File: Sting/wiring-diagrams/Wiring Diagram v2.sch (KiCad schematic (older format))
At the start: 14 parts

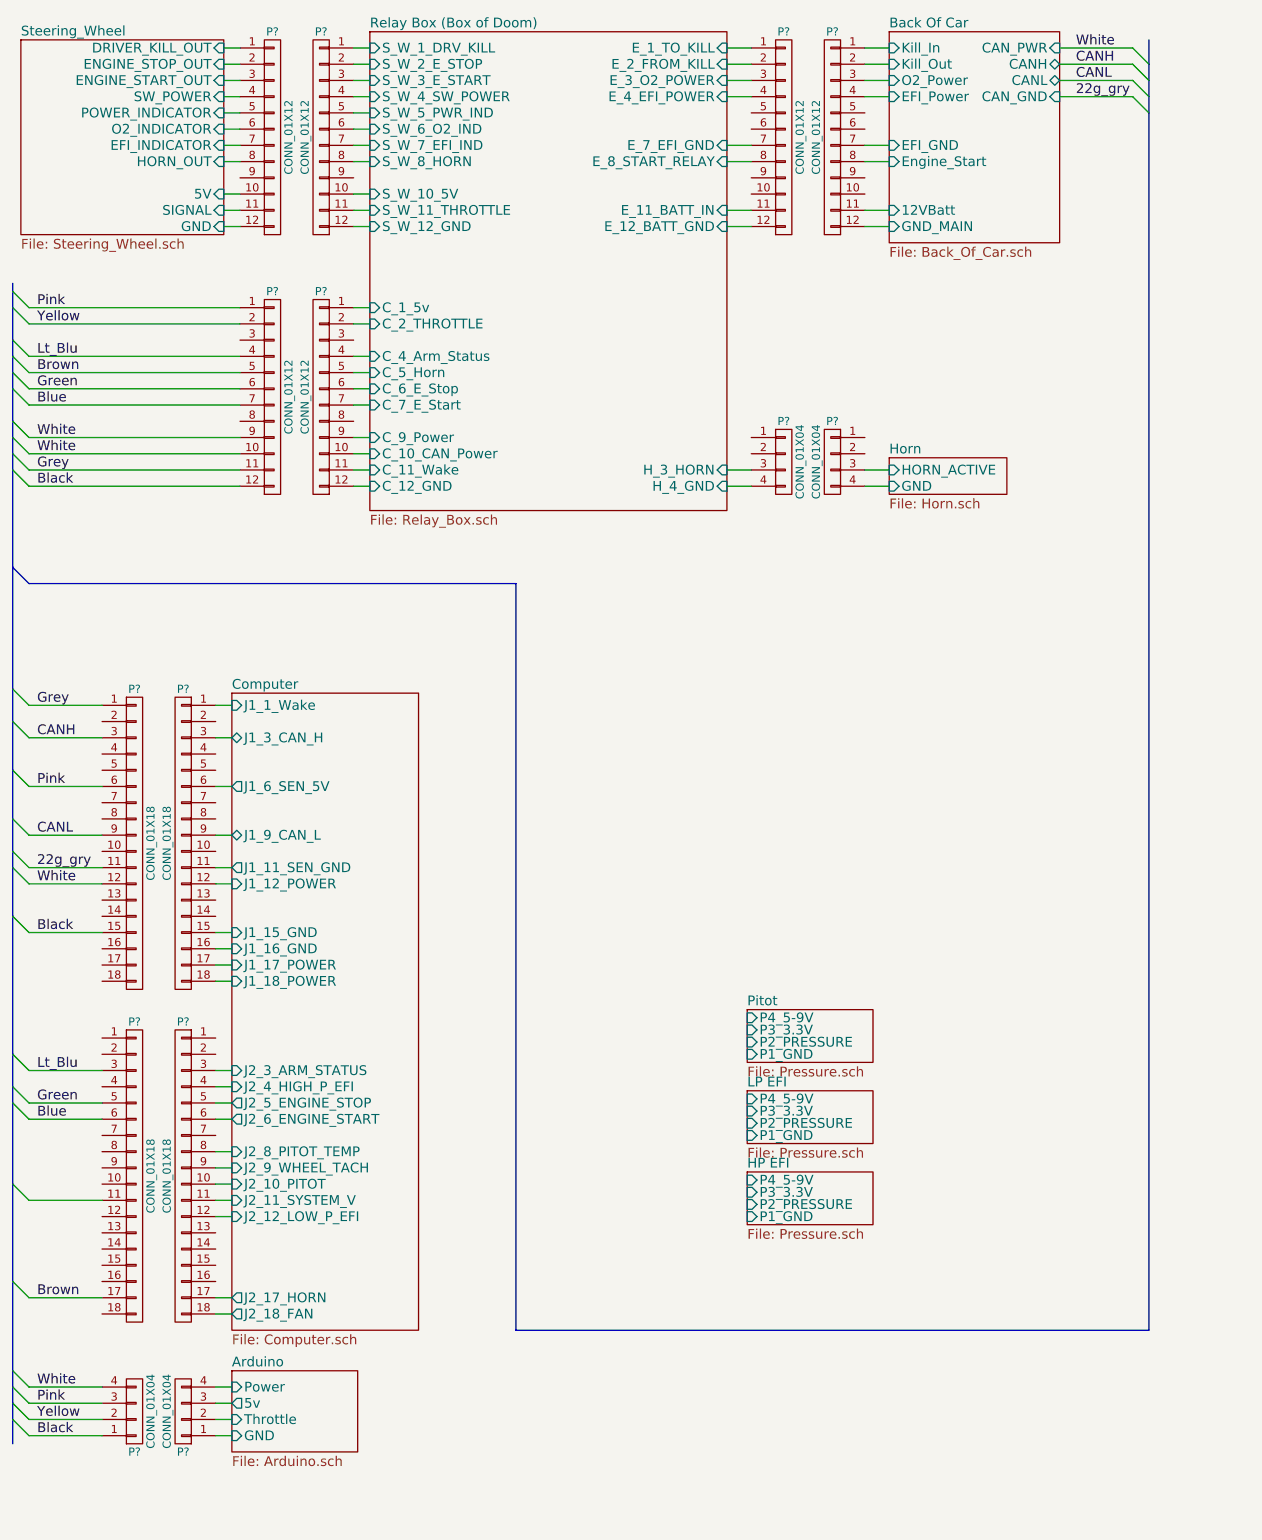
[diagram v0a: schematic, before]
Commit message: Lots of small changes, major change to the relay box layout.
Now using busses for the relay box.
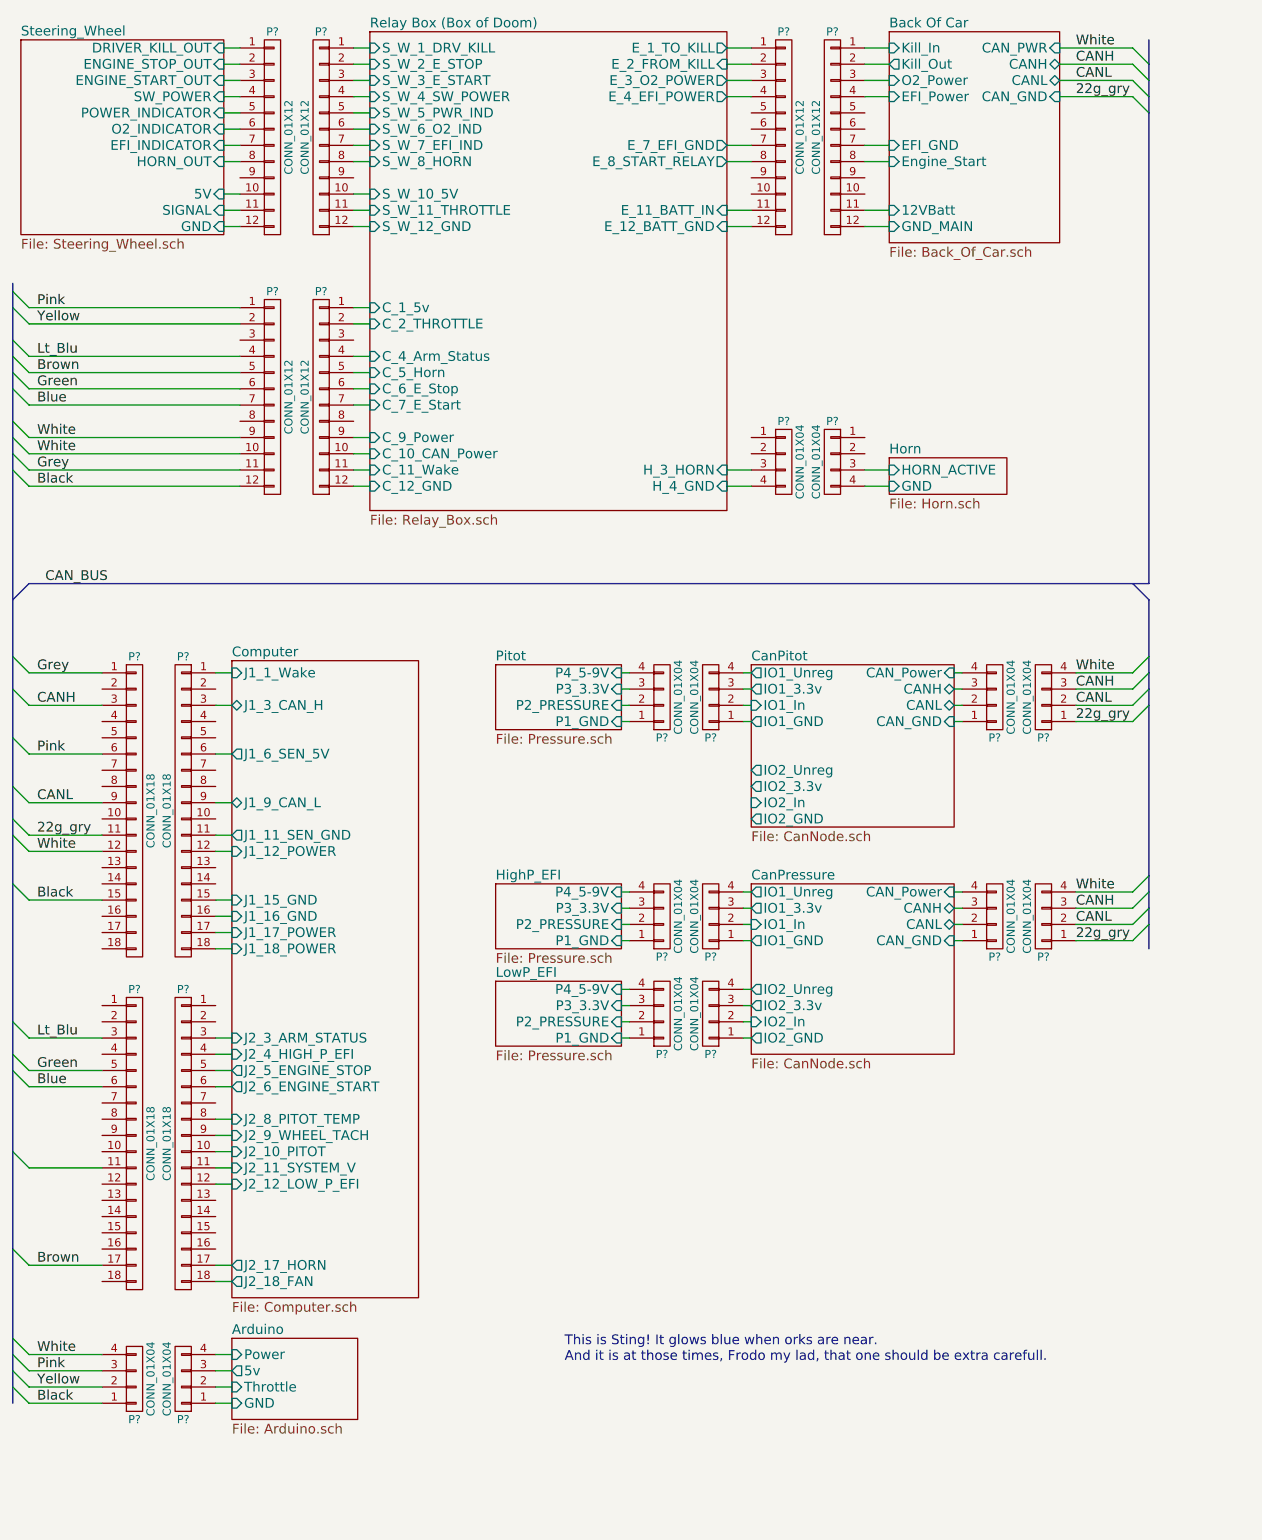
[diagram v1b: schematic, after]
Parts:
- added P? (x10): CONN_01X04, symbol CONN_01X04
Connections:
- net 22g_gry: now also P?.1 (P1), P?.1 (P1)
- net CANH: now also P?.3 (P3), P?.3 (P3)
- net CANL: now also P?.2 (P2), P?.2 (P2)
- net Pitot/P1_GND: now also P?.1 (P1)
- net Pitot/P2_PRESSURE: now also P?.2 (P2)
- net Pitot/P3_3.3V: now also P?.3 (P3)
- net Pitot/P4_5-9V: now also P?.4 (P4)
- net White: now also P?.4 (P4), P?.4 (P4)
- new net CanPitot/CANH: P?.3 (P3)
- new net CanPitot/CANL: P?.2 (P2)
- new net CanPitot/CAN_GND: P?.1 (P1)
- new net CanPitot/CAN_Power: P?.4 (P4)
- new net CanPitot/IO1_3.3v: P?.3 (P3)
- new net CanPitot/IO1_GND: P?.1 (P1)
- new net CanPitot/IO1_In: P?.2 (P2)
- new net CanPitot/IO1_Unreg: P?.4 (P4)
- new net CanPressure/CANH: P?.3 (P3)
- new net CanPressure/CANL: P?.2 (P2)
- new net CanPressure/CAN_GND: P?.1 (P1)
- new net CanPressure/CAN_Power: P?.4 (P4)
- new net CanPressure/IO1_3.3v: P?.3 (P3)
- new net CanPressure/IO1_GND: P?.1 (P1)
- new net CanPressure/IO1_In: P?.2 (P2)
- new net CanPressure/IO1_Unreg: P?.4 (P4)
- new net CanPressure/IO2_3.3v: P?.3 (P3)
- new net CanPressure/IO2_GND: P?.1 (P1)
- new net CanPressure/IO2_In: P?.2 (P2)
- new net CanPressure/IO2_Unreg: P?.4 (P4)
- new net HighP_EFI/P1_GND: P?.1 (P1)
- new net HighP_EFI/P2_PRESSURE: P?.2 (P2)
- new net HighP_EFI/P3_3.3V: P?.3 (P3)
- new net HighP_EFI/P4_5-9V: P?.4 (P4)
- new net LowP_EFI/P1_GND: P?.1 (P1)
- new net LowP_EFI/P2_PRESSURE: P?.2 (P2)
- new net LowP_EFI/P3_3.3V: P?.3 (P3)
- new net LowP_EFI/P4_5-9V: P?.4 (P4)
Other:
- note added: "This is Sting! It glows blue when orks are near.\nAnd it is at those times, Frodo my lad, that one should be extra carefull."
- moved on the sheet: P?

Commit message: Ah, its finished (I think).
Added the current sensor board into the wiring diagram, added titles to
all pages, tried to make everything look pretty.
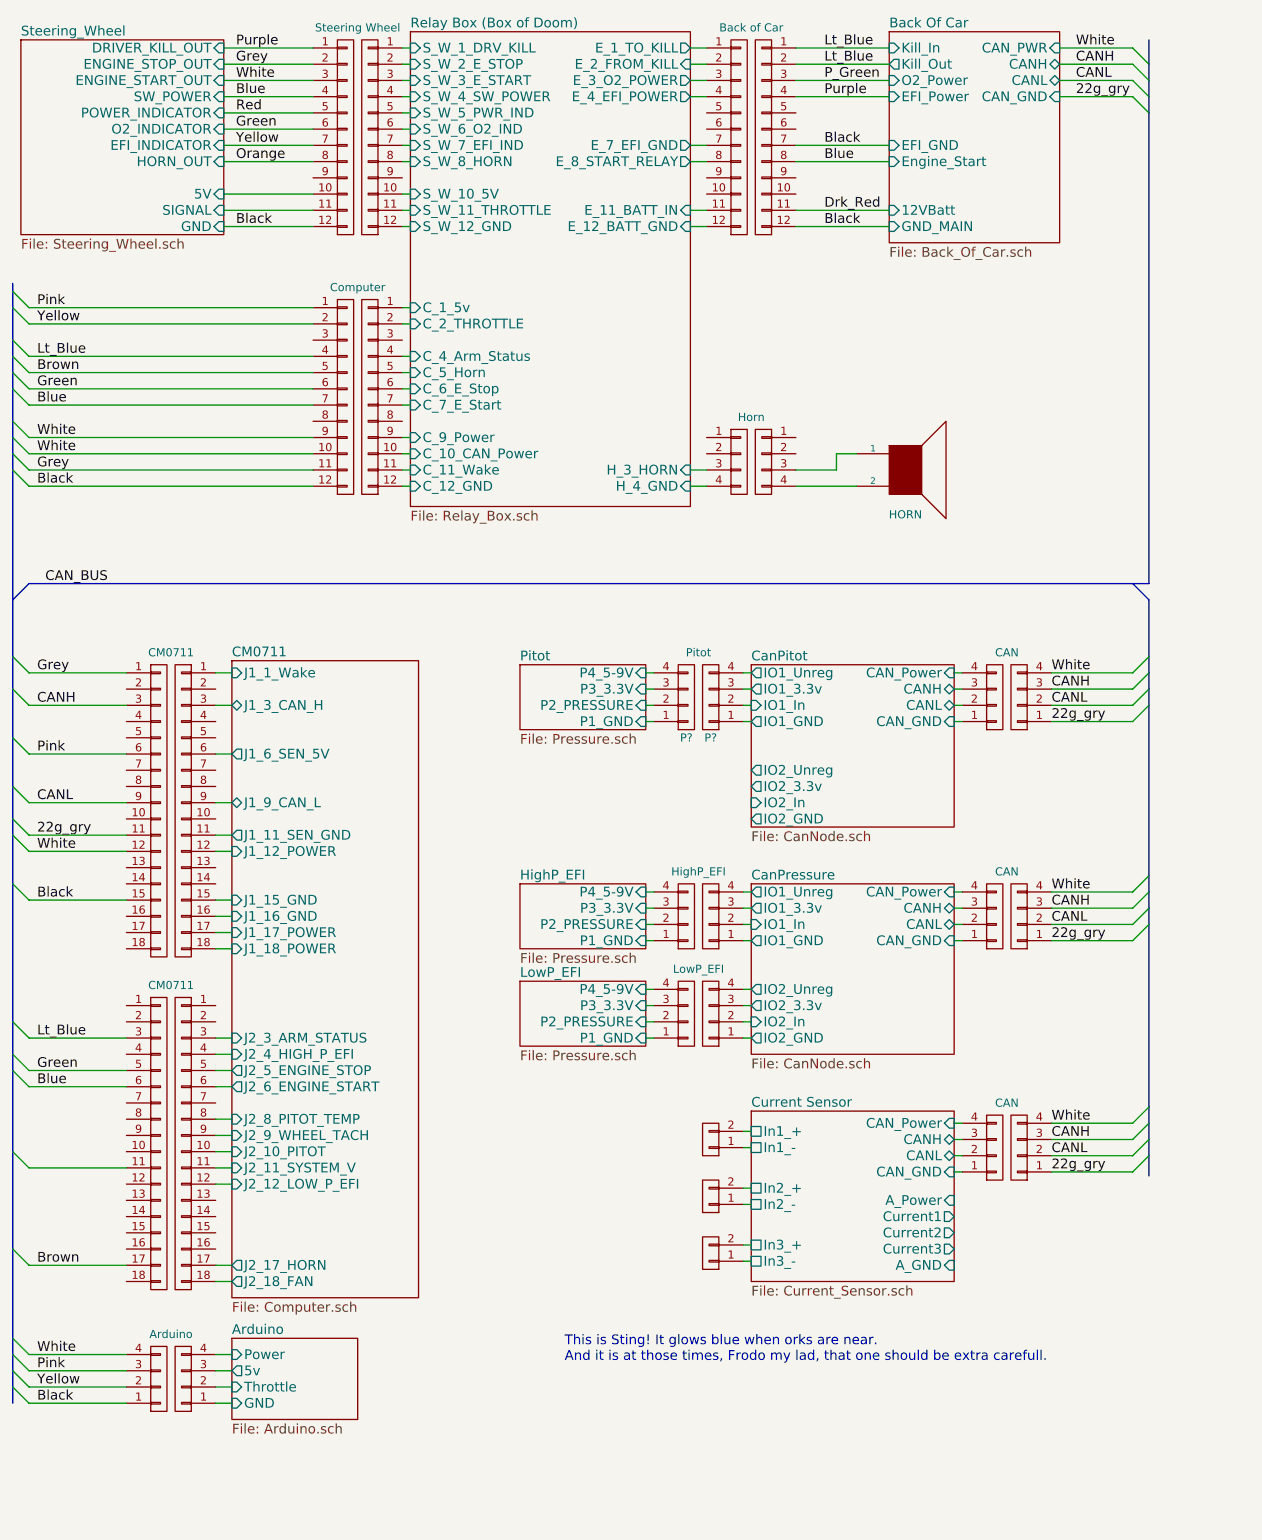
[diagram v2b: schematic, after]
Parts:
- added P? (x2): CAN, symbol CONN_01X04
- added P? (x3): CONN_01X02, symbol CONN_01X02
- added SP?: HORN, symbol SPEAKER
- P? (x4): value CONN_01X18 -> CM0711
- P? (x2): value CONN_01X12 -> Computer
- P? (x2): value CONN_01X12 -> Steering Wheel
- P? (x2): value CONN_01X12 -> Back of Car
- P? (x2): value CONN_01X04 -> Horn
- P? (x2): value CONN_01X04 -> Arduino
- P? (x2): value CONN_01X04 -> Pitot
- P? (x2): value CONN_01X04 -> HighP_EFI
- P? (x2): value CONN_01X04 -> LowP_EFI
- P? (x4): value CONN_01X04 -> CAN
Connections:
- net Back Of Car/EFI_GND is gone; now on net Black: P?.7 (P7)
- net Back Of Car/Engine_Start is gone; now on net Blue: P?.8 (P8)
- net Back Of Car/GND_MAIN is gone; now on net Black: P?.12 (P12)
- net Back Of Car/Kill_Out is gone; now on net Lt_Blue: P?.2 (P2)
- net Lt_Blu is gone; now on net Lt_Blue: P?.3 (P3), P?.4 (P4)
- net Steering_Wheel/DRIVER_KILL_OUT is gone; now on net Purple: P?.1 (P1)
- net Steering_Wheel/EFI_INDICATOR is gone; now on net Yellow: P?.7 (P7)
- net Steering_Wheel/ENGINE_START_OUT is gone; now on net White: P?.3 (P3)
- net Steering_Wheel/ENGINE_STOP_OUT is gone; now on net Grey: P?.2 (P2)
- net Steering_Wheel/GND is gone; now on net Black: P?.12 (P12)
- net Steering_Wheel/O2_INDICATOR is gone; now on net Green: P?.6 (P6)
- net Steering_Wheel/SW_POWER is gone; now on net Blue: P?.4 (P4)
- net 22g_gry: now also P?.1 (P1)
- net CANH: now also P?.3 (P3)
- net CANL: now also P?.2 (P2)
- net White: now also P?.4 (P4)
- net Back Of Car/12VBatt renamed Drk_Red
- net Back Of Car/EFI_Power renamed Purple
- net Back Of Car/Kill_In renamed Lt_Blue
- net Back Of Car/O2_Power renamed P_Green
- net Computer/J1_11_SEN_GND renamed CM0711/J1_11_SEN_GND
- net Computer/J1_12_POWER renamed CM0711/J1_12_POWER
- net Computer/J1_15_GND renamed CM0711/J1_15_GND
- net Computer/J1_16_GND renamed CM0711/J1_16_GND
- net Computer/J1_17_POWER renamed CM0711/J1_17_POWER
- net Computer/J1_18_POWER renamed CM0711/J1_18_POWER
- net Computer/J1_1_Wake renamed CM0711/J1_1_Wake
- net Computer/J1_3_CAN_H renamed CM0711/J1_3_CAN_H
- net Computer/J1_6_SEN_5V renamed CM0711/J1_6_SEN_5V
- net Computer/J1_9_CAN_L renamed CM0711/J1_9_CAN_L
- net Computer/J2_10_PITOT renamed CM0711/J2_10_PITOT
- net Computer/J2_11_SYSTEM_V renamed CM0711/J2_11_SYSTEM_V
- net Computer/J2_12_LOW_P_EFI renamed CM0711/J2_12_LOW_P_EFI
- net Computer/J2_17_HORN renamed CM0711/J2_17_HORN
- net Computer/J2_18_FAN renamed CM0711/J2_18_FAN
- net Computer/J2_3_ARM_STATUS renamed CM0711/J2_3_ARM_STATUS
- net Computer/J2_4_HIGH_P_EFI renamed CM0711/J2_4_HIGH_P_EFI
- net Computer/J2_5_ENGINE_STOP renamed CM0711/J2_5_ENGINE_STOP
- net Computer/J2_6_ENGINE_START renamed CM0711/J2_6_ENGINE_START
- net Computer/J2_8_PITOT_TEMP renamed CM0711/J2_8_PITOT_TEMP
- net Computer/J2_9_WHEEL_TACH renamed CM0711/J2_9_WHEEL_TACH
- net Horn/GND: no longer names the net of P?.4 (P4)
- net Horn/GND: now also SP?.2
- net Horn/HORN_ACTIVE: no longer names the net of P?.3 (P3)
- net Horn/HORN_ACTIVE: now also SP?.1
- net Steering_Wheel/HORN_OUT renamed Orange
- net Steering_Wheel/POWER_INDICATOR renamed Red
- new net Current Sensor/CANH: P?.3 (P3)
- new net Current Sensor/CANL: P?.2 (P2)
- new net Current Sensor/CAN_GND: P?.1 (P1)
- new net Current Sensor/CAN_Power: P?.4 (P4)
- new net Current Sensor/In1_+: P?.2 (P2)
- new net Current Sensor/In1_-: P?.1 (P1)
- new net Current Sensor/In2_+: P?.2 (P2)
- new net Current Sensor/In2_-: P?.1 (P1)
- new net Current Sensor/In3_+: P?.2 (P2)
- new net Current Sensor/In3_-: P?.1 (P1)
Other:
- moved on the sheet: P?

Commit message: Added arduino page, small cleanup elsewhere.
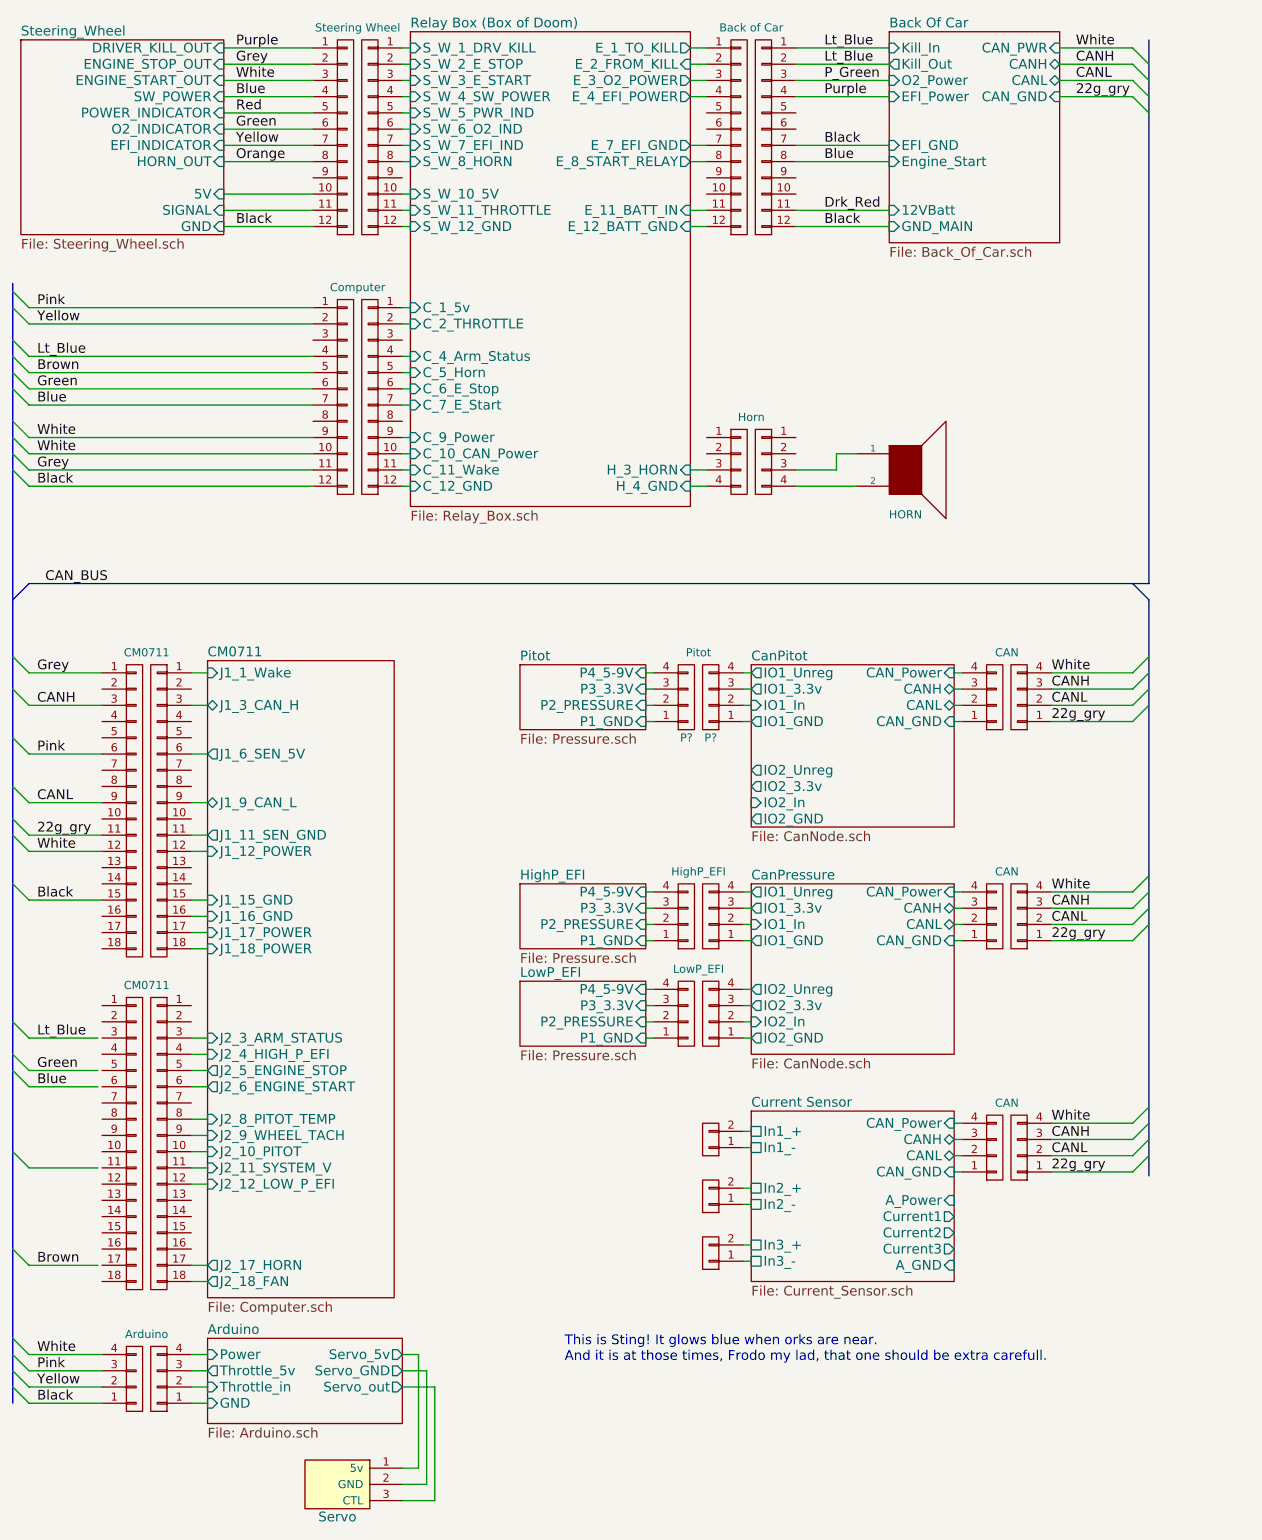
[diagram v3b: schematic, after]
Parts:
- added M?: Servo, symbol Servo
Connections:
- net Blue: no longer P?.6 (P6)
- net Brown: no longer P?.17 (P17)
- net Green: no longer P?.5 (P5)
- net Lt_Blue: no longer P?.3 (P3)
- net Arduino/5v renamed Arduino/Throttle_5v
- net Arduino/Throttle renamed Arduino/Throttle_in
- new net Arduino/Servo_5v: M?.1 (5v)
- new net Arduino/Servo_GND: M?.2 (GND)
- new net Arduino/Servo_out: M?.3 (CTL)
